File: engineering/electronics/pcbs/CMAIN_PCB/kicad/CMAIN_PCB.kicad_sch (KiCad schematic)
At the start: 79 parts, among them IC1 TSYS01, J1 RPI_5_WITH_SSQ-120-01-F-D, J10 1778719, J11 M9N-G4-3100, J12 B04B-JWPF-SK-R, J13 B04B-JWPF-SK-R, J14 XT30PW-F, J15 SM04B-GHS-TB_LF__SN_, J16 1778719, J17 SM03B-GHS-TB(LF)(SN), J19 1778719, J2 1778719, J21 1778719, J23 B04B-JWPF-SK-R, J24 1778719, J27 B04B-JWPF-SK-R, J29 B06B-JWPF-SK-R, J3 AXK6S00547YG, J30 B06B-JWPF-SK-R, J31 B06B-JWPF-SK-R, J32 B04B-JWPF-SK-R, J35 SM04B-GHS-TB_LF__SN_, J36 SM05B-GHS-TB_LF__SN_, J37 B04B-JWPF-SK-R, J38 B04B-JWPF-SK-R, J39 B04B-JWPF-SK-R, J4 AXK6S00547YG, J40 B04B-JWPF-SK-R, J41 SM06B-GHS-TB_LF__SN_, J43 B04B-JWPF-SK-R, J45 B04B-JWPF-SK-R, J46 B04B-JWPF-SK-R, J48 B04B-JWPF-SK-R, J49 B04B-JWPF-SK-R, J5 SM04B-GHS-TB_LF__SN_, J50 1814935, J52 B04B-JWPF-SK-R, J53 B04B-JWPF-SK-R, J55 B04B-JWPF-SK-R, J56 B04B-JWPF-SK-R, J57 B04B-JWPF-SK-R, J6 1778719, J7 SM04B-GHS-TB_LF__SN_, J8 B04B-JWPF-SK-R, J9 SM04B-GHS-TB_LF__SN_, U10 SMTSO25100CTJ, U11 SMTSO25100CTJ, U12 SMTSO25100CTJ, U3 SMTSOM380BTR, U6 SMTSOM380BTR, U7 SMTSOM380BTR, U8 SMTSOM380BTR, U9 SMTSO25100CTJ

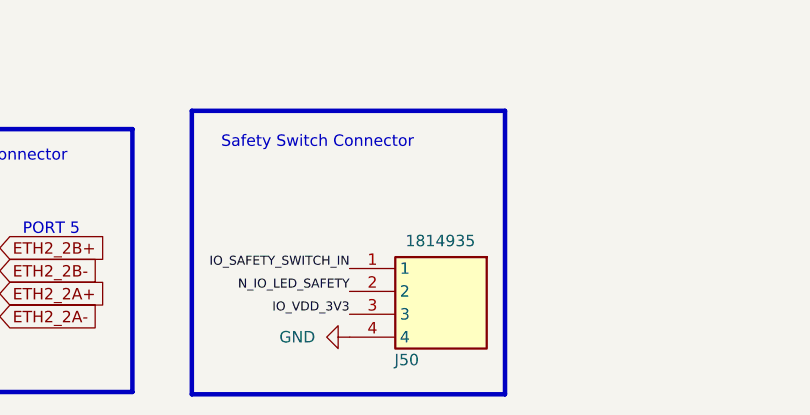
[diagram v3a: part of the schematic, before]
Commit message: electronics: integrate CMAIN STEP updates and consolidate footprints
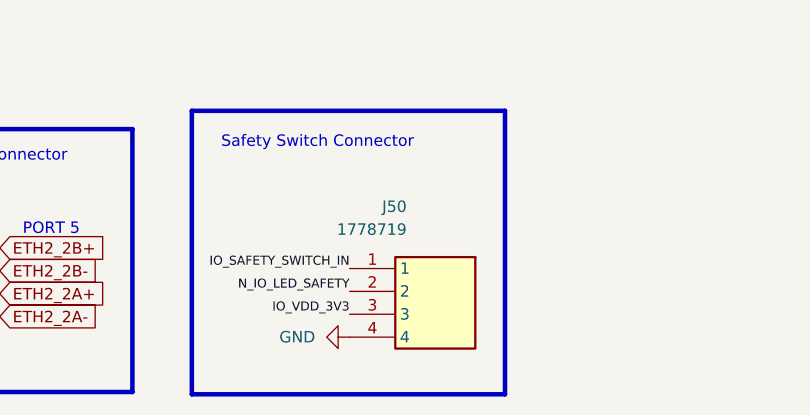
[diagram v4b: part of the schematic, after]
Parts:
- CN18, CN20, CN22, CN54: footprint EasyEDA_Lib_CMAIN:CONN-SMD_4P-P1.25_BM04B-GHS-TBT-LF-SN -> EasyEDA_Lib:fp_49628edcd6
- D5: footprint EasyEDA_Lib_CMAIN:SOT-23-6_L2.9-W1.6-P0.95-LS2.8-BL -> EasyEDA_Lib:SOT-23-6_L2.9-W1.6-P0.95-LS2.8-BL
- D8: footprint EasyEDA_Lib_CMAIN:SMA_L4.3-W2.6-LS5.0-FD -> EasyEDA_Lib:SMA_L4.3-W2.6-LS5.0-FD
- IC1: footprint Samacsys:QFN65P400X400X90-17N -> CMAIN_PCB:QFN65P400X400X90-17N
- J1: footprint Samacsys:SSM-120-XXX-DV -> CMAIN_PCB:SSM-120-XXX-DV
- J10, J16, J19, J2, J21, J24, J6: footprint Samacsys:1778719 -> CMAIN_PCB:1778719; symbol Samacsys:1778719 -> CMAIN_PCB:1778719
- J11: footprint Samacsys_kicad_sym:M9N-G4-3100 -> CMAIN_PCB:M9N-G4-3100
- J15, J5, J7, J9: symbol Samacsys:SM04B-GHS-TB_LF__SN_ -> CMAIN_PCB:fp_628ed3b7cf_LF__SN_
- J50: value 1814935 -> 1778719; footprint CMAIN_PCB:1814935 -> CMAIN_PCB:1778719; symbol Samacsys:1814935 -> CMAIN_PCB:1778719; Height 5.1 -> 7.65; Manufacturer_Part_Number 1814935 -> 1778719; Mouser Part Number 651-1814935 -> 651-1778719; Mouser Price/Stock https://www.mouser.co.uk/ProductDetail/Phoenix-Contact/1814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 -> https://www.mouser.co.uk/ProductDetail/Phoenix-Contact/1778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
- S2: footprint Samacsys:SLW9135352ASMT -> CMAIN_PCB:SLW9135352ASMT
- U10, U11, U12, U9: footprint Snapeda:SMD_BD5.6-L5.6-W5.6-D4.1 -> CMAIN_PCB:SMD_BD5.6-L5.6-W5.6-D4.1
- U19, U20, U21, U5: footprint EasyEDA_Lib_CMAIN:SMD_SMTSO3060CTJ -> EasyEDA_Lib:SMD_SMTSO3060CTJ
- U3, U6, U7, U8: footprint Snapeda:SMD_BD6.0-D4.2 -> CMAIN_PCB:SMD_BD6.0-D4.2
- USB33: footprint EasyEDA_Lib_CMAIN:USB-C-SMD_TYPEC-303-ACP16 -> EasyEDA_Lib:USB-C-SMD_TYPEC-303-ACP16
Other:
- moved on the sheet: J50
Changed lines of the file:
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@@
 			)
 		)
-		(property "Footprint" "EasyEDA_Lib_CMAIN:SMD_SMTSO3060CTJ"
+		(property "Footprint" "EasyEDA_Lib:SMD_SMTSO3060CTJ"
 			(at 137.16 216.662 0)
 			(hide yes)
@@
 	)
 	(symbol
-		(lib_id "Samacsys:SM04B-GHS-TB_LF__SN_")
+		(lib_id "CMAIN_PCB:fp_628ed3b7cf_LF__SN_")
 		(at 490.474 74.168 0)
 		(mirror y)
@@
 			)
 		)
-		(property "Footprint" "EasyEDA_Lib_CMAIN:SOT-23-6_L2.9-W1.6-P0.95-LS2.8-BL"
+		(property "Footprint" "EasyEDA_Lib:SOT-23-6_L2.9-W1.6-P0.95-LS2.8-BL"
 			(at 485.648 325.628 0)
 			(hide yes)
@@
 	)
 	(symbol
-		(lib_id "Samacsys:1778719")
+		(lib_id "CMAIN_PCB:1778719")
 		(at 358.394 166.116 0)
 		(mirror y)
@@
 			)
 		)
-		(property "Footprint" "Samacsys:1778719"
+		(property "Footprint" "CMAIN_PCB:1778719"
 			(at 341.884 261.366 0)
 			(hide yes)
@@
 			)
 		)
-		(property "Footprint" "Snapeda:SMD_BD5.6-L5.6-W5.6-D4.1"
+		(property "Footprint" "CMAIN_PCB:SMD_BD5.6-L5.6-W5.6-D4.1"
 			(at 170.434 351.79 0)
 			(hide yes)
@@
 	)
 	(symbol
-		(lib_id "Samacsys:SM04B-GHS-TB_LF__SN_")
+		(lib_id "CMAIN_PCB:fp_628ed3b7cf_LF__SN_")
 		(at 269.24 39.624 0)
 		(mirror y)
@@
 			)
 		)
-		(property "Footprint" "EasyEDA_Lib_CMAIN:CONN-SMD_4P-P1.25_BM04B-GHS-TBT-LF-SN"
+		(property "Footprint" "EasyEDA_Lib:fp_49628edcd6"
 			(at 285.75 151.13 0)
 			(hide yes)
@@
 	)
 	(symbol
-		(lib_id "Samacsys:1778719")
+		(lib_id "CMAIN_PCB:1778719")
 		(at 284.226 286.004 0)
 		(mirror y)
@@
 			)
 		)
-		(property "Footprint" "Samacsys:1778719"
+		(property "Footprint" "CMAIN_PCB:1778719"
 			(at 267.716 381.254 0)
 			(hide yes)
@@
 	)
 	(symbol
-		(lib_id "Samacsys:SM04B-GHS-TB_LF__SN_")
+		(lib_id "CMAIN_PCB:fp_628ed3b7cf_LF__SN_")
 		(at 536.956 74.422 0)
 		(mirror y)
@@
 			)
 		)
-		(property "Footprint" "Samacsys:QFN65P400X400X90-17N"
+		(property "Footprint" "CMAIN_PCB:QFN65P400X400X90-17N"
 			(at 481.33 227.076 0)
 			(hide yes)
@@
 	)
 	(symbol
-		(lib_id "Samacsys:1778719")
+		(lib_id "CMAIN_PCB:1778719")
 		(at 283.718 309.118 0)
 		(mirror y)
@@
 			)
 		)
-		(property "Footprint" "Samacsys:1778719"
+		(property "Footprint" "CMAIN_PCB:1778719"
 			(at 267.208 404.368 0)
 			(hide yes)
@@
 			)
 		)
-		(property "Footprint" "EasyEDA_Lib_CMAIN:CONN-SMD_4P-P1.25_BM04B-GHS-TBT-LF-SN"
+		(property "Footprint" "EasyEDA_Lib:fp_49628edcd6"
 			(at 265.43 158.75 0)
 			(hide yes)
@@
 			)
 		)
-		(property "Footprint" "Snapeda:SMD_BD5.6-L5.6-W5.6-D4.1"
+		(property "Footprint" "CMAIN_PCB:SMD_BD5.6-L5.6-W5.6-D4.1"
 			(at 170.434 346.71 0)
 			(hide yes)
@@
 			)
 		)
-		(property "Footprint" "Samacsys_kicad_sym:M9N-G4-3100"
+		(property "Footprint" "CMAIN_PCB:M9N-G4-3100"
 			(at 424.434 164.846 0)
 			(hide yes)
@@
 			)
 		)
-		(property "Footprint" "EasyEDA_Lib_CMAIN:SMD_SMTSO3060CTJ"
+		(property "Footprint" "EasyEDA_Lib:SMD_SMTSO3060CTJ"
 			(at 137.16 233.172 0)
 			(hide yes)
@@
 	)
 	(symbol
-		(lib_id "Samacsys:SM04B-GHS-TB_LF__SN_")
+		(lib_id "CMAIN_PCB:fp_628ed3b7cf_LF__SN_")
 		(at 446.532 68.072 0)
 		(unit 1)
@@
 			)
 		)
-		(property "Footprint" "Snapeda:SMD_BD6.0-D4.2"
+		(property "Footprint" "CMAIN_PCB:SMD_BD6.0-D4.2"
 			(at 416.052 104.902 0)
 			(hide yes)
@@
 	)
 	(symbol
-		(lib_id "Samacsys:1814935")
-		(at 360.426 367.284 0)
+		(lib_id "CMAIN_PCB:1778719")
+		(at 362.966 367.284 0)
 		(mirror y)
 		(unit 1)
@@
 		(dnp no)
 		(property "Reference" "J50"
-			(at 346.456 377.444 0)
+			(at 346.456 359.664 0)
 			(show_name no)
 			(do_not_autoplace no)
@@
 					(size 1.27 1.27)
 				)
+				(justify left top)
 			)
 		)
-		(property "Value" "1814935"
-			(at 354.076 363.474 0)
+		(property "Value" "1778719"
+			(at 346.456 362.204 0)
 			(show_name no)
 			(do_not_autoplace no)
@@
 			)
 		)
-		(property "Footprint" "CMAIN_PCB:1814935"
-			(at 343.916 461.264 0)
+		(property "Footprint" "CMAIN_PCB:1778719"
+			(at 346.456 462.204 0)
 			(hide yes)
 			(show_name no)
@@
 			)
 		)
-		(property "Datasheet" "http://www.phoenixcontact.com/de/produkte/1814935/pdf"
-			(at 343.916 561.594 0)
+		(property "Datasheet" "http://www.phoenixcontact.com/de/produkte/1778719/pdf"
+			(at 346.456 562.204 0)
 			(hide yes)
 			(show_name no)
@@
 			)
 		)
-		(property "Description" "PCB header, nominal cross section: 0.5 mm?, color: white, nominal current: 6 A, rated voltage (III/2): 160 V, contact surface: Tin, type of contact: Male connector, Number of potentials: 4, Number of rows: 1, Number of positions per row: 4, number of connections: 4, product range: PTSM 0,5/..-HH-SMD WH, pitch: 2.5 mm, mounting: SMD soldering, pin layout: Linear pad geometry, Stecksystem: COMBICON COMPACT PTSM, Locking: without, type of packaging: 32 mm wide tape"
-			(at 355.346 354.584 0)
+		(property "Description" "PCB header, nominal cross section: 0.5 mm?, color: white, nominal current: 6 A, rated voltage (III/2): 160 V, contact surface: Tin, type of contact: Male connector, Number of potentials: 4, Number of rows: 1, Number of positions per row: 4, number of connections: 4, product range: PTSM 0,5/..-HV-SMD WH, pitch: 2.5 mm, mounting: SMD soldering, pin layout: Linear pad geometry, solder pin [P]: 2 mm, Stecksystem: COMBICON COMPACT PTSM, Locking: without, type of packaging: 44 mm wide tape, Article with anti-rota"
+			(at 360.68 357.378 0)
 			(hide yes)
 			(show_name no)
@@
 			)
 		)
-		(property "Height" "5.1"
-			(at 343.916 762.254 0)
+		(property "Height" "7.65"
+			(at 346.456 762.204 0)
 			(hide yes)
 			(show_name no)
@@
 			)
 		)
-		(property "Mouser Part Number" "651-1814935"
-			(at 343.916 861.314 0)
+		(property "Mouser Part Number" "651-1778719"
+			(at 346.456 862.204 0)
 			(hide yes)
 			(show_name no)
@@
 			)
 		)
-		(property "Mouser Price/Stock" "https://www.mouser.co.uk/ProductDetail/Phoenix-Contact/1814935?qs=eTPcRhULBzz6VcWT1ftydw%3D%3D"
-			(at 343.916 961.644 0)
+		(property "Mouser Price/Stock" "https://www.mouser.co.uk/ProductDetail/Phoenix-Contact/1778719?qs=o1waKiAPAqfNyRuQw4b1ZA%3D%3D"
+			(at 346.456 962.204 0)
 			(hide yes)
 			(show_name no)
@@
 		)
 		(property "Manufacturer_Name" "Phoenix Contact"
-			(at 343.916 1061.974 0)
+			(at 346.456 1062.204 0)
 			(hide yes)
 			(show_name no)
@@
 			)
 		)
-		(property "Manufacturer_Part_Number" "1814935"
-			(at 343.916 1162.304 0)
+		(property "Manufacturer_Part_Number" "1778719"
+			(at 346.456 1162.204 0)
 			(hide yes)
 			(show_name no)
@@
 			)
 		)
-		(property "Footprint" "Samacsys:SLW9135352ASMT"
+		(property "Footprint" "CMAIN_PCB:SLW9135352ASMT"
 			(at 411.226 -55.372 0)
 			(hide yes)
@@
 			)
 		)
-		(property "Footprint" "EasyEDA_Lib_CMAIN:USB-C-SMD_TYPEC-303-ACP16"
+		(property "Footprint" "EasyEDA_Lib:USB-C-SMD_TYPEC-303-ACP16"
 			(at 425.958 325.628 0)
 			(hide yes)
@@
 			)
 		)
-		(property "Footprint" "Snapeda:SMD_BD5.6-L5.6-W5.6-D4.1"
+		(property "Footprint" "CMAIN_PCB:SMD_BD5.6-L5.6-W5.6-D4.1"
 			(at 170.434 354.33 0)
 			(hide yes)
@@
 			)
 		)
-		(property "Footprint" "Snapeda:SMD_BD6.0-D4.2"
+		(property "Footprint" "CMAIN_PCB:SMD_BD6.0-D4.2"
 			(at 416.052 102.362 0)
 			(hide yes)
@@
 	)
 	(symbol
-		(lib_id "Samacsys:1778719")
+		(lib_id "CMAIN_PCB:1778719")
 		(at 358.394 128.778 0)
 		(mirror y)
@@
 			)
 		)
-		(property "Footprint" "Samacsys:1778719"
+		(property "Footprint" "CMAIN_PCB:1778719"
 			(at 341.884 224.028 0)
 			(hide yes)
@@
 			)
 		)
-		(property "Footprint" "Snapeda:SMD_BD6.0-D4.2"
+		(property "Footprint" "CMAIN_PCB:SMD_BD6.0-D4.2"
 			(at 416.052 97.282 0)
 			(hide yes)
@@
 			)
 		)
-		(property "Footprint" "Snapeda:SMD_BD6.0-D4.2"
+		(property "Footprint" "CMAIN_PCB:SMD_BD6.0-D4.2"
 			(at 416.052 99.822 0)
 			(hide yes)
@@
 	)
 	(symbol
-		(lib_id "Samacsys:1778719")
+		(lib_id "CMAIN_PCB:1778719")
 		(at 358.394 150.876 0)
 		(mirror y)
@@
 			)
 		)
-		(property "Footprint" "Samacsys:1778719"
+		(property "Footprint" "CMAIN_PCB:1778719"
 			(at 341.884 244.856 0)
 			(hide yes)
@@
 			)
 		)
-		(property "Footprint" "EasyEDA_Lib_CMAIN:CONN-SMD_4P-P1.25_BM04B-GHS-TBT-LF-SN"
+		(property "Footprint" "EasyEDA_Lib:fp_49628edcd6"
 			(at 306.07 156.21 0)
 			(hide yes)
@@
 			)
 		)
-		(property "Footprint" "EasyEDA_Lib_CMAIN:CONN-SMD_4P-P1.25_BM04B-GHS-TBT-LF-SN"
+		(property "Footprint" "EasyEDA_Lib:fp_49628edcd6"
 			(at 242.57 153.67 0)
 			(hide yes)
@@
 			)
 		)
-		(property "Footprint" "EasyEDA_Lib_CMAIN:SMA_L4.3-W2.6-LS5.0-FD"
+		(property "Footprint" "EasyEDA_Lib:SMA_L4.3-W2.6-LS5.0-FD"
 			(at 453.898 309.118 0)
 			(hide yes)
@@
 			)
 		)
-		(property "Footprint" "EasyEDA_Lib_CMAIN:SMD_SMTSO3060CTJ"
+		(property "Footprint" "EasyEDA_Lib:SMD_SMTSO3060CTJ"
 			(at 137.16 222.25 0)
 			(hide yes)
@@
 			)
 		)
-		(property "Footprint" "Snapeda:SMD_BD5.6-L5.6-W5.6-D4.1"
+		(property "Footprint" "CMAIN_PCB:SMD_BD5.6-L5.6-W5.6-D4.1"
 			(at 170.434 349.25 0)
 			(hide yes)
@@
 	)
 	(symbol
-		(lib_id "Samacsys:1778719")
+		(lib_id "CMAIN_PCB:1778719")
 		(at 358.394 110.998 0)
 		(mirror y)
@@
 			)
 		)
-		(property "Footprint" "Samacsys:1778719"
+		(property "Footprint" "CMAIN_PCB:1778719"
 			(at 341.884 206.248 0)
 			(hide yes)
@@
 	)
 	(symbol
-		(lib_id "Samacsys:1778719")
+		(lib_id "CMAIN_PCB:1778719")
 		(at 278.384 364.998 0)
 		(unit 1)
@@
 			)
 		)
-		(property "Footprint" "Samacsys:1778719"
+		(property "Footprint" "CMAIN_PCB:1778719"
 			(at 294.894 460.248 0)
 			(hide yes)
@@
 			)
 		)
-		(property "Footprint" "EasyEDA_Lib_CMAIN:SMD_SMTSO3060CTJ"
+		(property "Footprint" "EasyEDA_Lib:SMD_SMTSO3060CTJ"
 			(at 137.16 227.584 0)
 			(hide yes)
@@
 			)
 		)
-		(property "Footprint" "Samacsys:SSM-120-XXX-DV"
+		(property "Footprint" "CMAIN_PCB:SSM-120-XXX-DV"
 			(at 210.058 376.428 0)
 			(hide yes)
